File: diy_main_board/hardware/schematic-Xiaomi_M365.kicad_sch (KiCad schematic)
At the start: 8 parts, among them J1 Connector_1, J2 Connector_2, U1 ESP32-S3-DevKitC

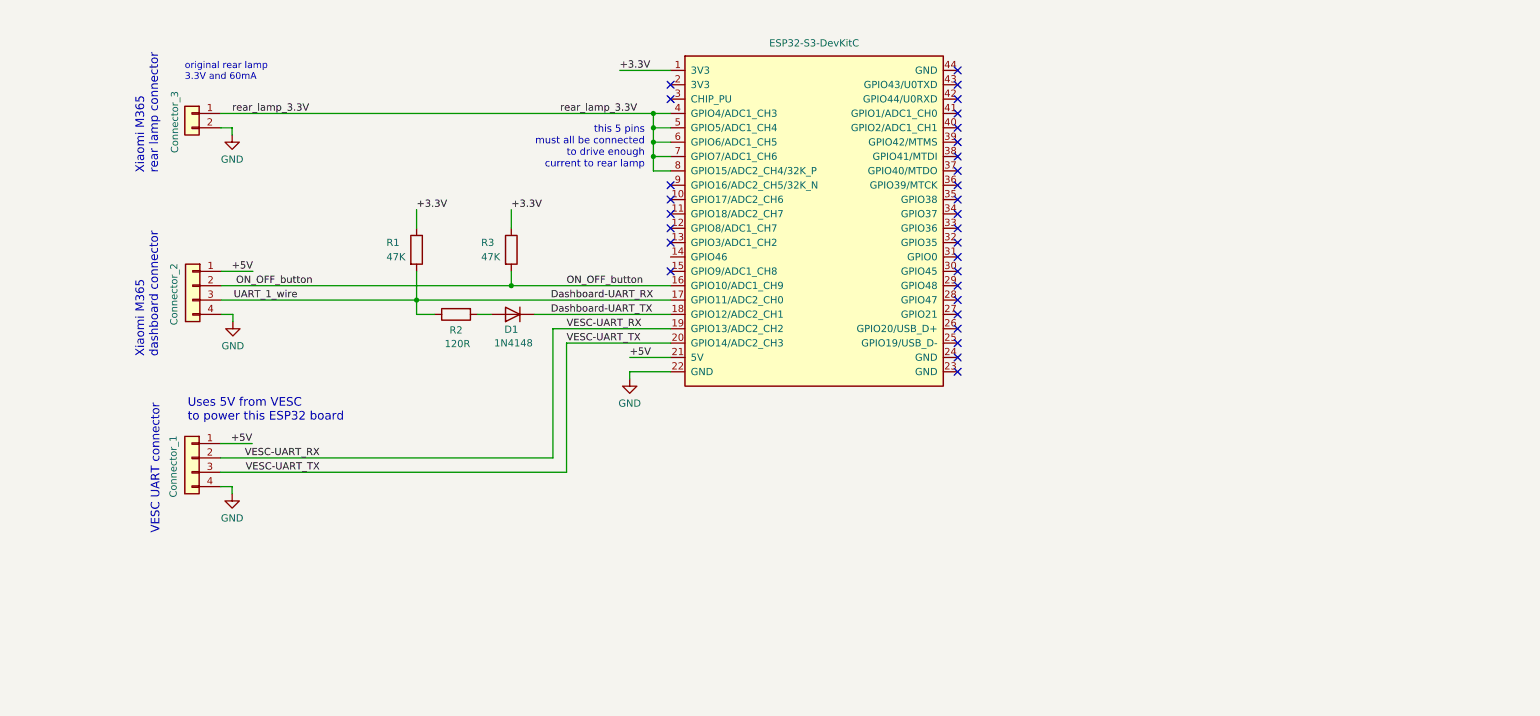
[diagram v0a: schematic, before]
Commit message: Updated Fiido Q1S and Xiaomi_M365 main boards schematics
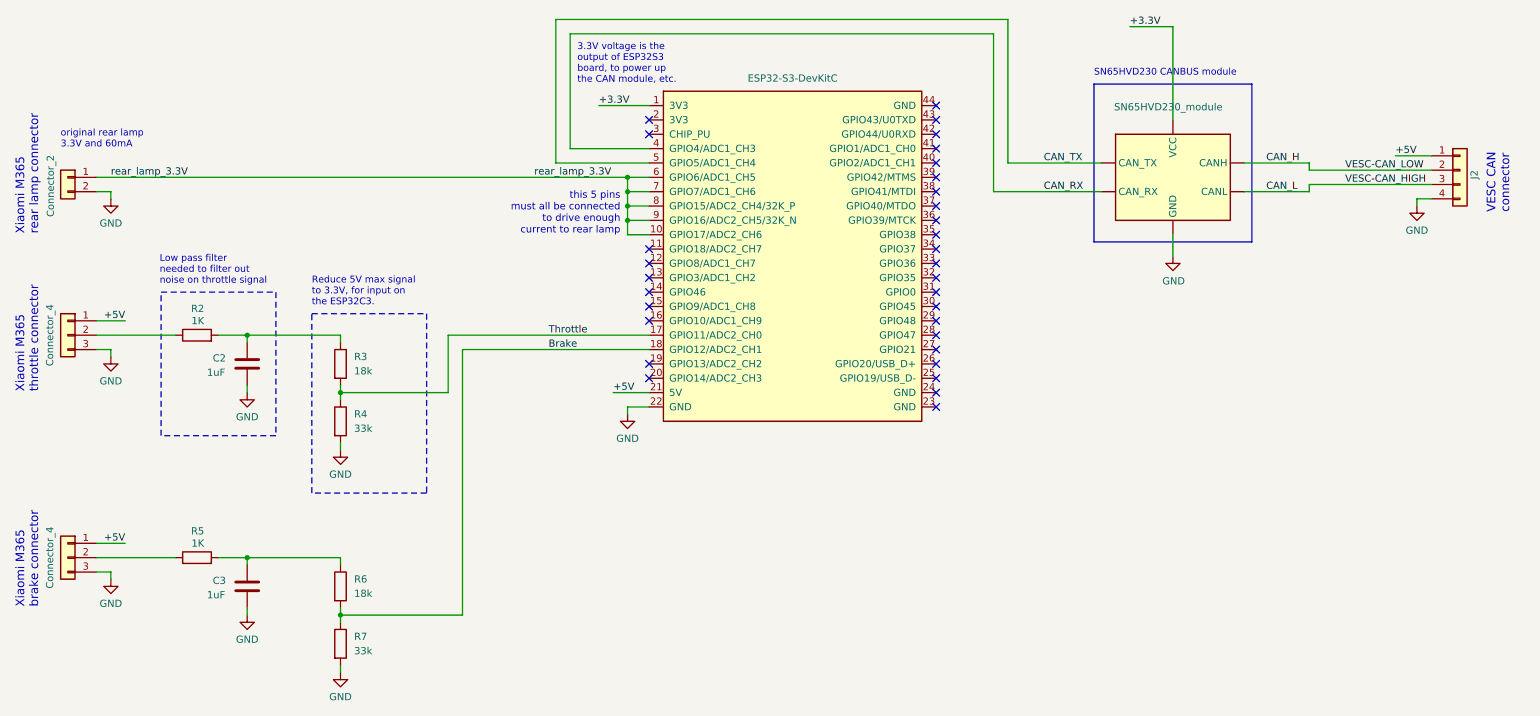
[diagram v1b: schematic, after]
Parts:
- removed Connector_3: ~, symbol Connector_Generic:Conn_01x02
- removed D1: 1N4148, Diode_THT:D_DO-35_SOD27_P7.62mm_Horizontal, symbol Diode:1N4148
- removed J1: Connector_1, symbol Connector_Generic:Conn_01x04
- removed R1: 47K, symbol Device:R
- added C2, C3: 1uF, symbol Device:C
- added Connector_2: ~, symbol Connector_Generic:Conn_01x02
- added J1, J3: Connector_4, symbol Connector_Generic:Conn_01x03
- added R4, R7: 33k, symbol Device:R
- added R5: 1K, symbol Device:R
- added R6: 18k, symbol Device:R
- added U2: SN65HVD230_module, symbol TJA1050:TJA1050_module
- J2: value Connector_2 -> Conn_01x04
- R2: value 120R -> 1K
- R3: value 47K -> 18k
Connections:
- net +3.3V: now also U2. (VCC); no longer R3.1
- net +5V: now also J1.1 (Pin_1), J3.1 (Pin_1)
- net GND: now also C2.2, C3.2, Connector_2.2 (Pin_2), J1.3 (Pin_3), J3.3 (Pin_3), R4.2, R7.2, U2. (VCC)
- net rear_lamp_3.3V: now also U1.10 (GPIO17/ADC2_CH6), U1.9 (GPIO16/ADC2_CH5/32K_N), Connector_2.1 (Pin_1); no longer U1.4 (GPIO4/ADC1_CH3), U1.5 (GPIO5/ADC1_CH4)
- net at R2.2: now also R3.1, C2.1
- removed net Dashboard-UART_RX: J2.3 (Pin_3), R2.1, U1.17 (GPIO11/ADC2_CH0)
- net Dashboard-UART_TX renamed Brake
- net Brake: now also R6.2, R7.1
- removed net ON_OFF_button: J2.2 (Pin_2), R3.2, U1.16 (GPIO10/ADC1_CH9)
- net VESC-UART_RX: no longer names the net of U1.19 (GPIO13/ADC2_CH2)
- net VESC-UART_TX: no longer names the net of U1.20 (GPIO14/ADC2_CH3)
- new net: J3.2 (Pin_2), R5.1
- new net: C3.1, R5.2, R6.1
- new net: J1.2 (Pin_2), R2.1
- new net CAN_H: J2.2 (Pin_2), U2. (VCC)
- new net CAN_L: J2.3 (Pin_3), U2. (VCC)
- new net CAN_RX: U1.4 (GPIO4/ADC1_CH3), U2. (VCC)
- new net CAN_TX: U1.5 (GPIO5/ADC1_CH4), U2. (VCC)
- new net Throttle: R3.2, R4.1, U1.17 (GPIO11/ADC2_CH0)
- no-connect marks 30 -> 32
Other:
- note added: "3.3V voltage is the output of ESP32S3 board, to power up the CAN module, etc."
- note added: "Low pass filter needed to filter out noise on throttle signal"
- note added: "Reduce 5V max signal to 3.3V, for input on the ESP32C3."
- note added: "SN65HVD230 CANBUS module"
- note added: "VESC CAN connector"
- note added: "Xiaomi M365 brake connector"
- note added: "Xiaomi M365 throttle connector"
- note removed: "Uses 5V from VESC to power this ESP32 board"
- note removed: "VESC UART connector"
- note removed: "Xiaomi M365 dashboard connector"

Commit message: Updateschematic components anotation
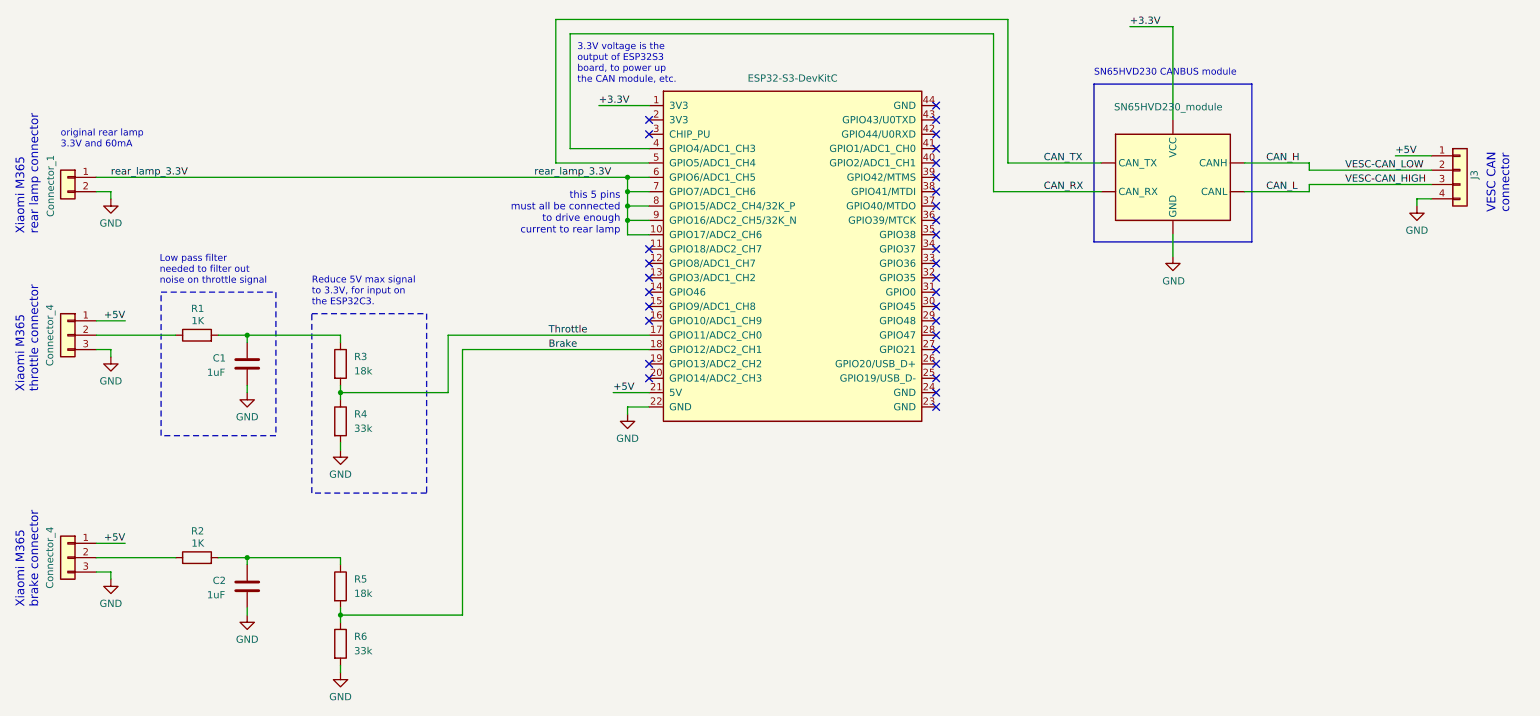
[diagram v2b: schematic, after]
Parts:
- renumbered C2 to C1, C3 to C2, Connector_2 to Connector_1, J3 to J2, J2 to J3, R2 to R1, R5 to R2, R6 to R5, R7 to R6
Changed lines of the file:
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@@
 		(on_board yes)
 		(dnp no)
-		(property "Reference" "#PWR03"
+		(property "Reference" "#PWR01"
 			(at 99.06 132.08 0)
 			(effects
@@
 			(project "schematic-Xiaomi_M365"
 				(path "/b96fe6ac-3535-4455-ab88-ed77f5e46d6e"
-					(reference "#PWR03")
+					(reference "#PWR01")
 					(unit 1)
 				)
@@
 		(on_board yes)
 		(dnp no)
-		(property "Reference" "J3"
+		(property "Reference" "J2"
 			(at 91.44 181.864 0)
 			(effects
@@
 			(project "schematic-Xiaomi_M365"
 				(path "/b96fe6ac-3535-4455-ab88-ed77f5e46d6e"
-					(reference "J3")
+					(reference "J2")
 					(unit 1)
 				)
@@
 		(on_board yes)
 		(dnp no)
-		(property "Reference" "C3"
+		(property "Reference" "C2"
 			(at 117.094 193.294 0)
 			(effects
@@
 			(project "schematic-Xiaomi_M365"
 				(path "/b96fe6ac-3535-4455-ab88-ed77f5e46d6e"
-					(reference "C3")
+					(reference "C2")
 					(unit 1)
 				)
@@
 		(on_board yes)
 		(dnp no)
-		(property "Reference" "J2"
+		(property "Reference" "J3"
 			(at 340.36 120.6499 90)
 			(effects
@@
 			(project ""
 				(path "/b96fe6ac-3535-4455-ab88-ed77f5e46d6e"
-					(reference "J2")
+					(reference "J3")
 					(unit 1)
 				)
@@
 		(on_board yes)
 		(dnp no)
-		(property "Reference" "R2"
+		(property "Reference" "R1"
 			(at 115.57 145.161 90)
 			(effects
@@
 			(project "schematic-Xiaomi_M365"
 				(path "/b96fe6ac-3535-4455-ab88-ed77f5e46d6e"
-					(reference "R2")
+					(reference "R1")
 					(unit 1)
 				)
@@
 		(on_board yes)
 		(dnp no)
-		(property "Reference" "#PWR05"
+		(property "Reference" "#PWR04"
 			(at 123.19 166.37 0)
 			(effects
@@
 			(project "schematic-Xiaomi_M365"
 				(path "/b96fe6ac-3535-4455-ab88-ed77f5e46d6e"
-					(reference "#PWR05")
+					(reference "#PWR04")
 					(unit 1)
 				)
@@
 		(on_board yes)
 		(dnp no)
-		(property "Reference" "R6"
+		(property "Reference" "R5"
 			(at 142.113 193.04 0)
 			(effects
@@
 			(project "schematic-Xiaomi_M365"
 				(path "/b96fe6ac-3535-4455-ab88-ed77f5e46d6e"
-					(reference "R6")
+					(reference "R5")
 					(unit 1)
 				)
@@
 		(on_board yes)
 		(dnp no)
-		(property "Reference" "#PWR010"
+		(property "Reference" "#PWR03"
 			(at 99.06 199.39 0)
 			(effects
@@
 			(project "schematic-Xiaomi_M365"
 				(path "/b96fe6ac-3535-4455-ab88-ed77f5e46d6e"
-					(reference "#PWR010")
+					(reference "#PWR03")
 					(unit 1)
 				)
@@
 		(on_board yes)
 		(dnp no)
-		(property "Reference" "C2"
+		(property "Reference" "C1"
 			(at 117.094 153.924 0)
 			(effects
@@
 			(project "schematic-Xiaomi_M365"
 				(path "/b96fe6ac-3535-4455-ab88-ed77f5e46d6e"
-					(reference "C2")
+					(reference "C1")
 					(unit 1)
 				)
@@
 		(on_board yes)
 		(dnp no)
-		(property "Reference" "#PWR09"
+		(property "Reference" "#PWR010"
 			(at 330.2 133.35 0)
 			(effects
@@
 			(project "schematic-Xiaomi_M365"
 				(path "/b96fe6ac-3535-4455-ab88-ed77f5e46d6e"
-					(reference "#PWR09")
+					(reference "#PWR010")
 					(unit 1)
 				)
@@
 		(on_board yes)
 		(dnp no)
-		(property "Reference" "#PWR012"
+		(property "Reference" "#PWR07"
 			(at 139.7 215.9 0)
 			(effects
@@
 			(project "schematic-Xiaomi_M365"
 				(path "/b96fe6ac-3535-4455-ab88-ed77f5e46d6e"
-					(reference "#PWR012")
+					(reference "#PWR07")
 					(unit 1)
 				)
@@
 		(on_board yes)
 		(dnp no)
-		(property "Reference" "Connector_2"
+		(property "Reference" "Connector_1"
 			(at 88.392 123.444 90)
 			(effects
@@
 			(project "schematic-Xiaomi_M365"
 				(path "/b96fe6ac-3535-4455-ab88-ed77f5e46d6e"
-					(reference "Connector_2")
+					(reference "Connector_1")
 					(unit 1)
 				)
@@
 		(on_board yes)
 		(dnp no)
-		(property "Reference" "R7"
+		(property "Reference" "R6"
 			(at 142.113 203.2 0)
 			(effects
@@
 			(project "schematic-Xiaomi_M365"
 				(path "/b96fe6ac-3535-4455-ab88-ed77f5e46d6e"
-					(reference "R7")
+					(reference "R6")
 					(unit 1)
 				)
@@
 		(on_board yes)
 		(dnp no)
-		(property "Reference" "#PWR04"
+		(property "Reference" "#PWR02"
 			(at 99.06 160.02 0)
 			(effects
@@
 			(project "schematic-Xiaomi_M365"
 				(path "/b96fe6ac-3535-4455-ab88-ed77f5e46d6e"
-					(reference "#PWR04")
+					(reference "#PWR02")
 					(unit 1)
 				)
@@
 		(on_board yes)
 		(dnp no)
-		(property "Reference" "#PWR07"
+		(property "Reference" "#PWR08"
 			(at 190.5 170.18 0)
 			(effects
@@
 			(project "schematic-Xiaomi_M365"
 				(path "/b96fe6ac-3535-4455-ab88-ed77f5e46d6e"
-					(reference "#PWR07")
+					(reference "#PWR08")
 					(unit 1)
 				)
@@
 		(on_board yes)
 		(dnp no)
-		(property "Reference" "#PWR08"
+		(property "Reference" "#PWR09"
 			(at 287.02 142.24 0)
 			(effects
@@
 			(project "schematic-Xiaomi_M365"
 				(path "/b96fe6ac-3535-4455-ab88-ed77f5e46d6e"
-					(reference "#PWR08")
+					(reference "#PWR09")
 					(unit 1)
 				)
@@
 		(on_board yes)
 		(dnp no)
-		(property "Reference" "#PWR011"
+		(property "Reference" "#PWR05"
 			(at 123.19 205.74 0)
 			(effects
@@
 			(project "schematic-Xiaomi_M365"
 				(path "/b96fe6ac-3535-4455-ab88-ed77f5e46d6e"
-					(reference "#PWR011")
+					(reference "#PWR05")
 					(unit 1)
 				)
@@
 		(on_board yes)
 		(dnp no)
-		(property "Reference" "R5"
+		(property "Reference" "R2"
 			(at 115.57 184.531 90)
 			(effects
@@
 			(project "schematic-Xiaomi_M365"
 				(path "/b96fe6ac-3535-4455-ab88-ed77f5e46d6e"
-					(reference "R5")
-					(unit 1)
-				)
+					(reference "R2")
+					(unit 1)
+				)

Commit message: Added latest schematic as tested on a real scooter
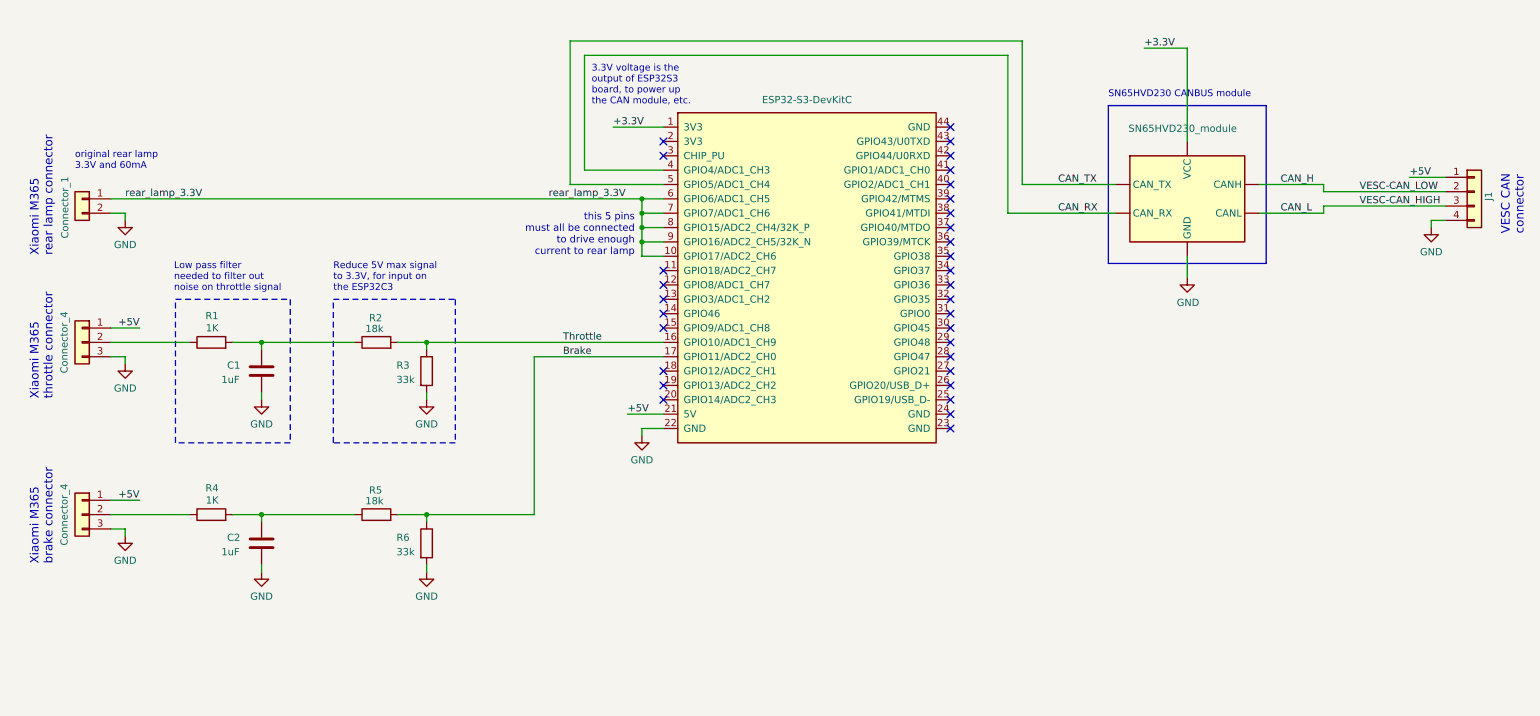
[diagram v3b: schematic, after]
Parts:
- renumbered J3 to J1, J1 to J2, J2 to J3, R3 to R2, R4 to R3, R2 to R4, U2 to U1, U1 to U2
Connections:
- net Brake: now also U2.17 (GPIO11/ADC2_CH0); no longer U2.18 (GPIO12/ADC2_CH1)
- net Throttle: now also U2.16 (GPIO10/ADC1_CH9); no longer U2.17 (GPIO11/ADC2_CH0)
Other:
- note added: "Reduce 5V max signal to 3.3V, for input on the ESP32C3"
- note removed: "Reduce 5V max signal to 3.3V, for input on the ESP32C3."
- moved on the sheet: C1, C2, Connector_1, J1, R1, R2, R3, R4
